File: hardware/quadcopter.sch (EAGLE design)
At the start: 99 parts, among them J1 HEADER-4POS-0.1IN-FEMALE-SMD-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, J2 HEADER-10POSTH-254X10, J3 HEADER-4POS-0.1IN-FEMALE, J4 AVR_SPI_PRG_6-SMD, M1 MOTOR_PADS_GND-MOLEX-SMD, M2 MOTOR_PADS_GND-MOLEX-SMD, M3 MOTOR_PADS_GND-MOLEX-SMD, M4 MOTOR_PADS_GND-MOLEX-SMD, P1 PROPELLOR-45MM, P2 PROPELLOR-45MM, P3 PROPELLOR-45MM, P4 PROPELLOR-45MM, Q1 N-MOSFET-SI2302DS, Q12 N-MOSFET-SI2302DS, Q2 N-MOSFET-SI2302DS, Q3 N-MOSFET-SI2302DS, Q4 N-MOSFET-SI2302DS, Q6 N-MOSFET-SI2302DS, Q8 N-MOSFET-SI2302DS, Q9 N-MOSFET-SI2302DS, SW1 PUSHBUTTON_-4.5X4.5, U1 ATMEGA128RFA1, U2 IMU_LSM9DS1-LSM9DS1, Y1 CRYSTAL5X3

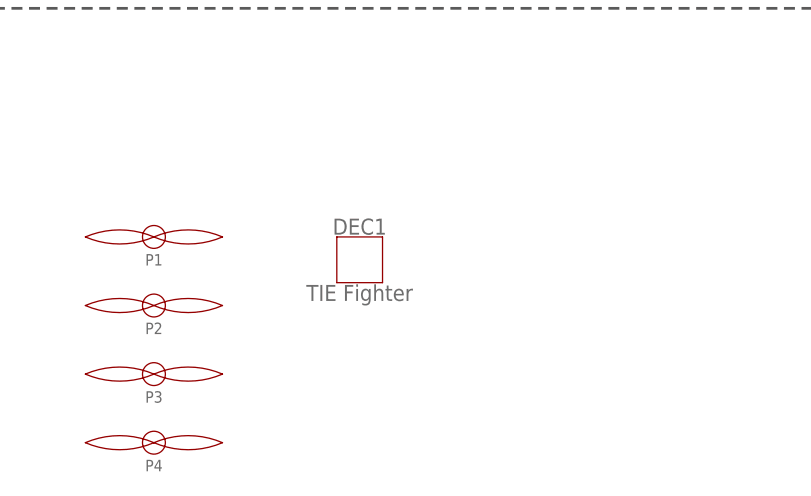
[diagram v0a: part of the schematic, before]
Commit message: Replaced local refs to `custom_michael_shao` lbr with team version
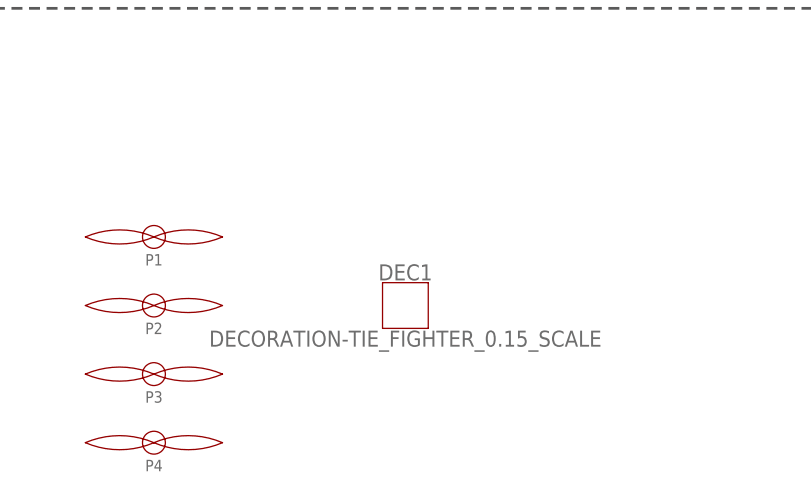
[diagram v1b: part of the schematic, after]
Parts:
- DEC1: value TIE Fighter -> DECORATION-TIE_FIGHTER_0.15_SCALE
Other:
- moved on the sheet: DEC1

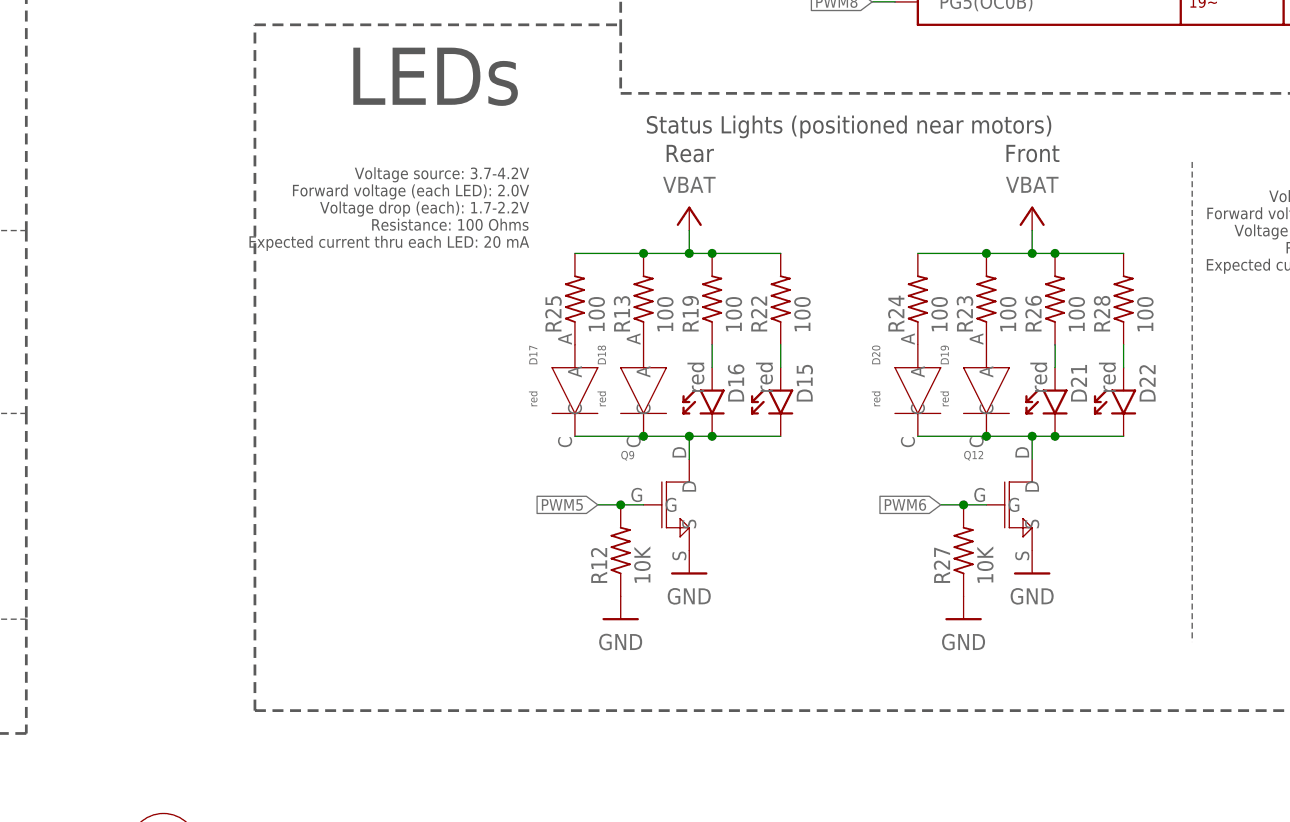
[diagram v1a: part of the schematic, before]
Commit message: Removed unnecessary LEDs
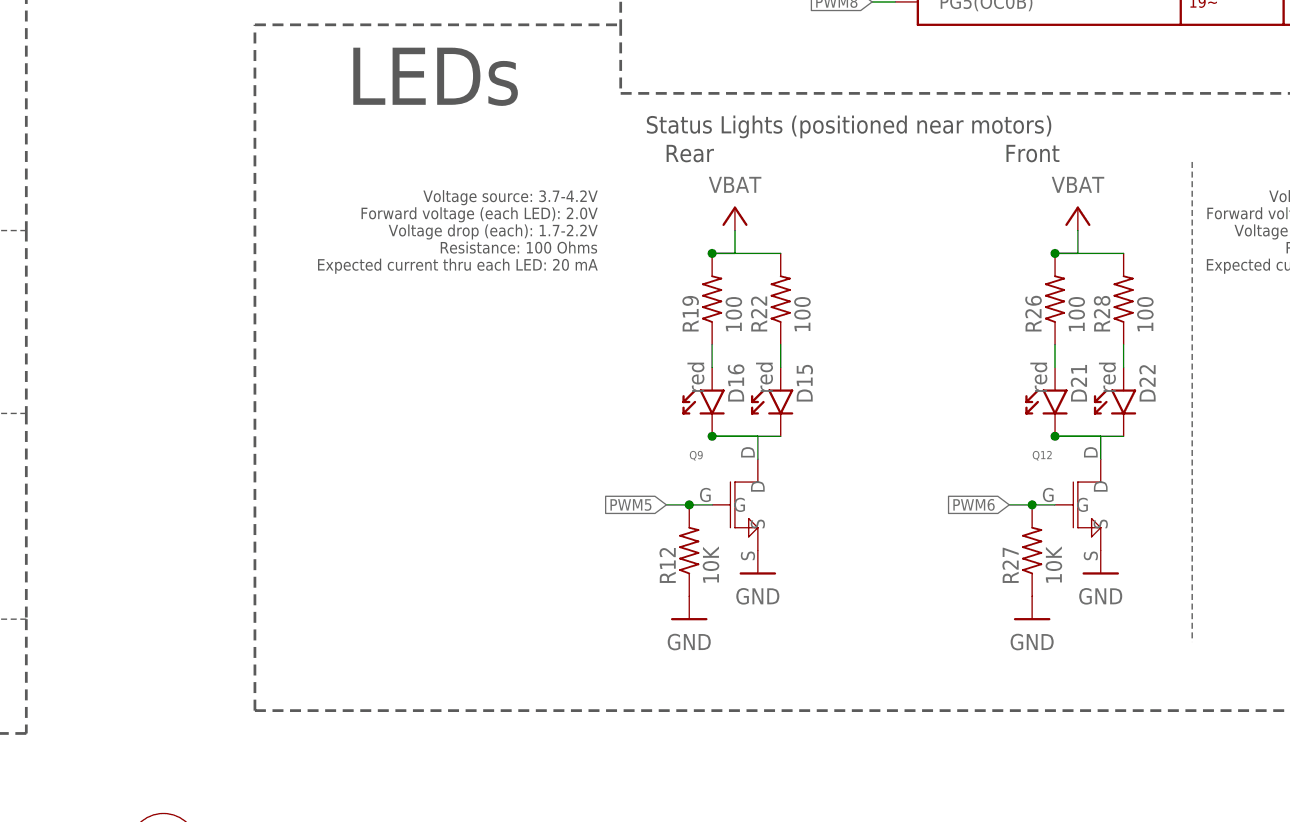
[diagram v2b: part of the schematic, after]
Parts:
- removed D17, D18, D19, D20: red, custom_michael_shao:LED_RED-LTST-C170EKT
- removed R13, R23, R24, R25: 100, quadparts_prebuilt_2022:RESISTOR_SMD-2012-0805-100
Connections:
- removed net N$24: D17.A, R25.1
- removed net N$25: D18.A, R13.1
- removed net N$38: D19.A, R23.1
- removed net N$39: D20.A, R24.1
- net N$35: no longer D17.C, D18.C
- net N$40: no longer D19.C, D20.C
- net VBAT: no longer R13.2, R23.2, R24.2, R25.2
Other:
- moved on the sheet: Q12, Q9, R12, R27

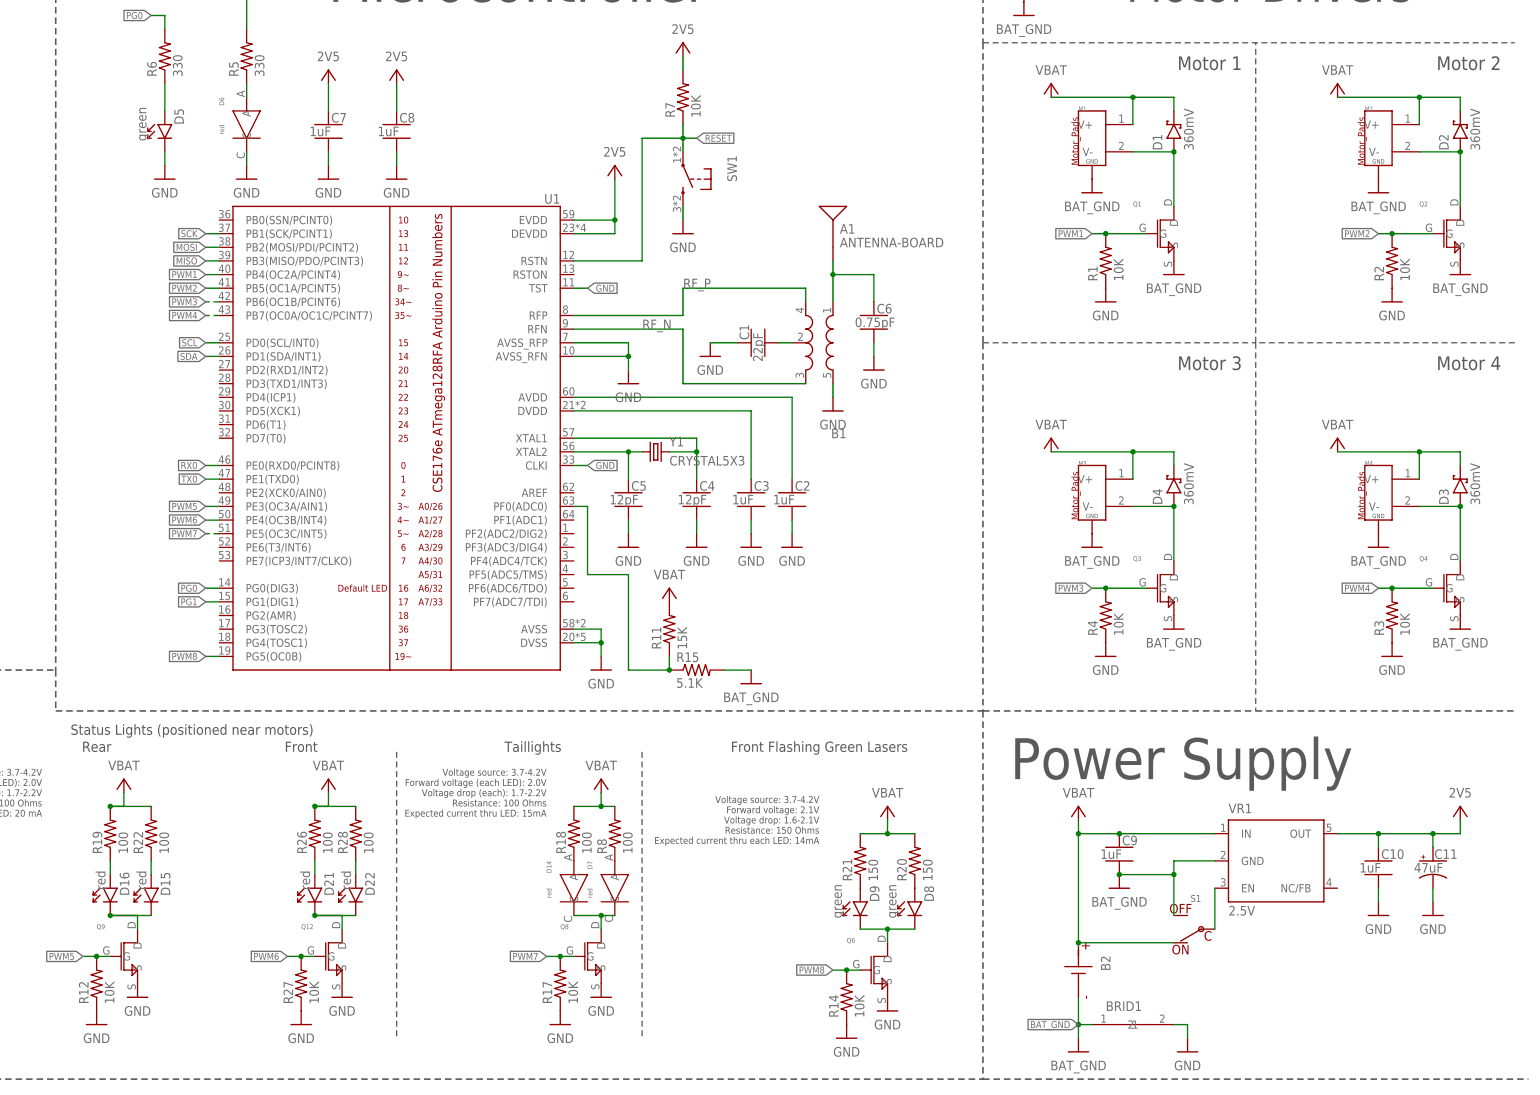
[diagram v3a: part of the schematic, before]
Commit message: Implementing changes from design review
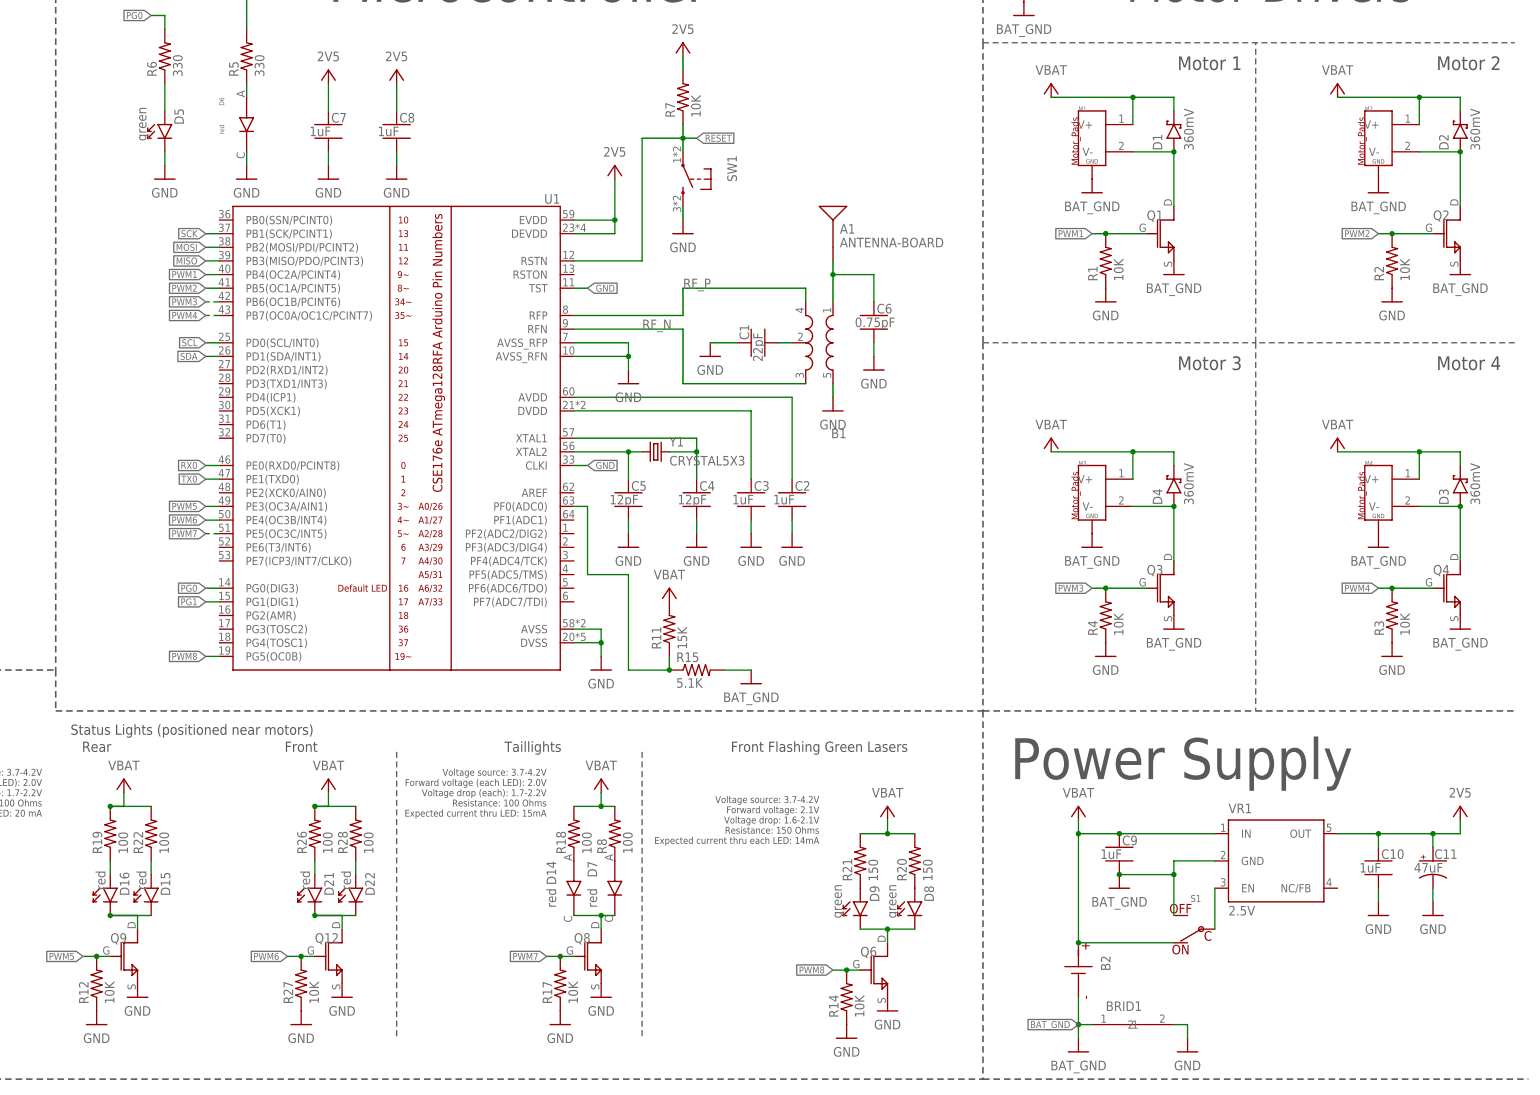
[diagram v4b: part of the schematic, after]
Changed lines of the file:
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@@
 <setting verticaltext="up"/>
 </settings>
-<grid distance="0.1" unitdist="inch" unit="inch" style="lines" multiple="1" display="no" altdistance="0.01" altunitdist="inch" altunit="inch"/>
+<grid distance="0.1" unitdist="inch" unit="inch" style="lines" multiple="1" display="yes" altdistance="0.01" altunitdist="inch" altunit="inch"/>
 <layers>
 <layer number="1" name="Top" color="4" fill="1" visible="no" active="no"/>
@@
 </instance>
 <instance part="Q1" gate="G$1" x="363.22" y="218.44" smashed="yes">
-<attribute name="NAME" x="355.6" y="223.52" size="0.9" layer="95" font="vector"/>
+<attribute name="NAME" x="358.14" y="220.98" size="1.778" layer="95" font="vector"/>
 </instance>
 <instance part="Q2" gate="G$1" x="416.56" y="218.44" smashed="yes">
-<attribute name="NAME" x="408.94" y="223.52" size="0.9" layer="95" font="vector"/>
+<attribute name="NAME" x="411.48" y="220.98" size="1.778" layer="95" font="vector"/>
 </instance>
 <instance part="Q3" gate="G$1" x="363.22" y="152.4" smashed="yes">
-<attribute name="NAME" x="355.6" y="157.48" size="0.9" layer="95" font="vector"/>
+<attribute name="NAME" x="358.14" y="154.94" size="1.778" layer="95" font="vector"/>
 </instance>
 <instance part="Q4" gate="G$1" x="416.56" y="152.4" smashed="yes">
-<attribute name="NAME" x="408.94" y="157.48" size="0.9" layer="95" font="vector"/>
+<attribute name="NAME" x="411.48" y="154.94" size="1.778" layer="95" font="vector"/>
 </instance>
 <instance part="D6" gate="G$1" x="190.5" y="238.76" smashed="yes" rot="R270">
@@
 </instance>
 <instance part="Q6" gate="G$1" x="309.88" y="81.28" smashed="yes">
-<attribute name="NAME" x="302.26" y="86.36" size="0.9" layer="95" font="vector"/>
+<attribute name="NAME" x="304.8" y="83.82" size="1.778" layer="95" font="vector"/>
 </instance>
 <instance part="GND40" gate="1" x="309.88" y="73.66" smashed="yes">
@@
 </instance>
 <instance part="Q9" gate="G$1" x="170.18" y="83.82" smashed="yes">
-<attribute name="NAME" x="162.56" y="88.9" size="0.9" layer="95" font="vector"/>
+<attribute name="NAME" x="165.1" y="86.36" size="1.778" layer="95" font="vector"/>
 </instance>
 <instance part="GND45" gate="1" x="170.18" y="76.2" smashed="yes">
@@
 </instance>
 <instance part="Q12" gate="G$1" x="208.28" y="83.82" smashed="yes">
-<attribute name="NAME" x="200.66" y="88.9" size="0.9" layer="95" font="vector"/>
+<attribute name="NAME" x="203.2" y="86.36" size="1.778" layer="95" font="vector"/>
 </instance>
 <instance part="GND49" gate="1" x="208.28" y="76.2" smashed="yes">
@@
 </instance>
 <instance part="Q8" gate="G$1" x="256.54" y="83.82" smashed="yes">
-<attribute name="NAME" x="248.92" y="88.9" size="0.9" layer="95" font="vector"/>
+<attribute name="NAME" x="251.46" y="86.36" size="1.778" layer="95" font="vector"/>
 </instance>
 <instance part="GND44" gate="1" x="256.54" y="76.2" smashed="yes">
@@
 </instance>
 <instance part="D14" gate="G$1" x="251.46" y="96.52" smashed="yes" rot="R270">
-<attribute name="NAME" x="246.38" y="101.6" size="0.9" layer="95" font="vector" rot="R270"/>
-<attribute name="VALUE" x="246.38" y="96.52" size="0.9" layer="96" font="vector" rot="R270"/>
+<attribute name="NAME" x="246.38" y="101.6" size="1.778" layer="95" font="vector" rot="R270"/>
+<attribute name="VALUE" x="246.38" y="96.52" size="1.778" layer="96" font="vector" rot="R270"/>
 </instance>
 <instance part="R18" gate="G$1" x="251.46" y="106.68" smashed="yes" rot="R90">
@@
 </instance>
 <instance part="D7" gate="G$1" x="259.08" y="96.52" smashed="yes" rot="R270">
-<attribute name="NAME" x="254" y="101.6" size="0.9" layer="95" font="vector" rot="R270"/>
-<attribute name="VALUE" x="254" y="96.52" size="0.9" layer="96" font="vector" rot="R270"/>
+<attribute name="NAME" x="254" y="101.6" size="1.778" layer="95" font="vector" rot="R270"/>
+<attribute name="VALUE" x="254" y="96.52" size="1.778" layer="96" font="vector" rot="R270"/>
 </instance>
 <instance part="P1" gate="G$1" x="132.08" y="35.56" smashed="yes">
@@
 <label x="160.02" y="83.82" size="1.27" layer="95" rot="R180" xref="yes"/>
 <pinref part="R12" gate="G$1" pin="2"/>
+<junction x="162.56" y="83.82"/>
 <pinref part="Q9" gate="G$1" pin="G"/>
-<junction x="162.56" y="83.82"/>
 </segment>
 </net>
@@
 <label x="198.12" y="83.82" size="1.27" layer="95" rot="R180" xref="yes"/>
 <pinref part="R27" gate="G$1" pin="2"/>
+<junction x="200.66" y="83.82"/>
 <pinref part="Q12" gate="G$1" pin="G"/>
-<junction x="200.66" y="83.82"/>
 </segment>
 </net>
@@
 <pinref part="D15" gate="G$1" pin="C"/>
 <pinref part="D16" gate="G$1" pin="C"/>
+<junction x="165.1" y="91.44"/>
 <pinref part="Q9" gate="G$1" pin="D"/>
-<junction x="165.1" y="91.44"/>
 </segment>
 </net>
@@
 <pinref part="D22" gate="G$1" pin="C"/>
 <pinref part="D21" gate="G$1" pin="C"/>
+<junction x="203.2" y="91.44"/>
 <pinref part="Q12" gate="G$1" pin="D"/>
-<junction x="203.2" y="91.44"/>
-</segment>
-</net>
+</segment>
+</net>

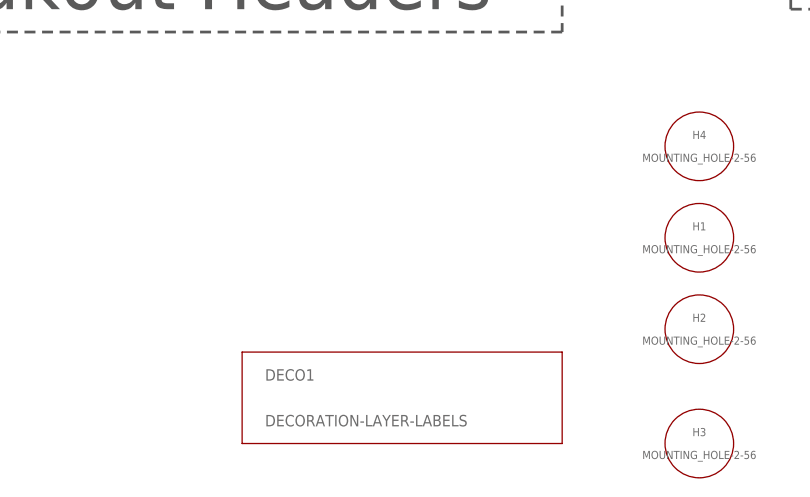
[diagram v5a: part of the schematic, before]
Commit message: Add class logo, "created by" and date to the silkscreen
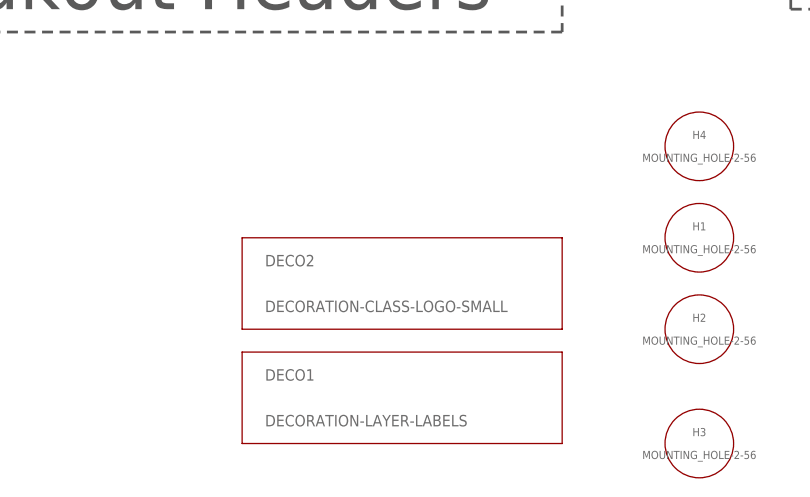
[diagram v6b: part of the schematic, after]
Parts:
- added DECO2: DECORATION-CLASS-LOGO-SMALL, quadparts_prebuilt_2022:DECORATION-CLASS-LOGO-SMALL
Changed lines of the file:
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@@
 <setting verticaltext="up"/>
 </settings>
-<grid distance="0.1" unitdist="inch" unit="inch" style="lines" multiple="1" display="yes" altdistance="0.01" altunitdist="inch" altunit="inch"/>
+<grid distance="0.1" unitdist="inch" unit="inch" style="lines" multiple="1" display="no" altdistance="0.01" altunitdist="inch" altunit="inch"/>
 <layers>
 <layer number="1" name="Top" color="4" fill="1" visible="no" active="no"/>
@@
 <part name="GND28" library="quadparts_prebuilt_2022" library_urn="urn:adsk.wipprod:fs.file:vf.VudH_-qgS-enOFMGlZoxrw" deviceset="BAT_GND" device=""/>
 <part name="DEC1" library="custom_michael_shao" library_urn="urn:adsk.wipprod:fs.file:vf.WEX53KctTd223gU3vuBSuw" deviceset="DECORATION" device="-TIE_FIGHTER_0.15_SCALE"/>
+<part name="DECO2" library="quadparts_prebuilt_2022" library_urn="urn:adsk.wipprod:fs.file:vf.VudH_-qgS-enOFMGlZoxrw" deviceset="DECORATION" device="-CLASS-LOGO-SMALL"/>
 </parts>
 <sheets>
@@
 <attribute name="VALUE" x="160.02" y="25.146" size="1.778" layer="96" align="top-center"/>
 </instance>
+<instance part="DECO2" gate="G$1" x="55.88" y="30.48" smashed="yes">
+<attribute name="NAME" x="55.88" y="33.02" size="1.27" layer="95" font="vector" align="center-left"/>
+<attribute name="VALUE" x="55.88" y="27.94" size="1.27" layer="96" font="vector" align="center-left"/>
+</instance>
 </instances>
